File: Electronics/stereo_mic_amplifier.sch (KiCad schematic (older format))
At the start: 26 parts, among them P1 mic_L, P2 mic_R, P3 batt, P4 CONN_01X03, U1 TL072

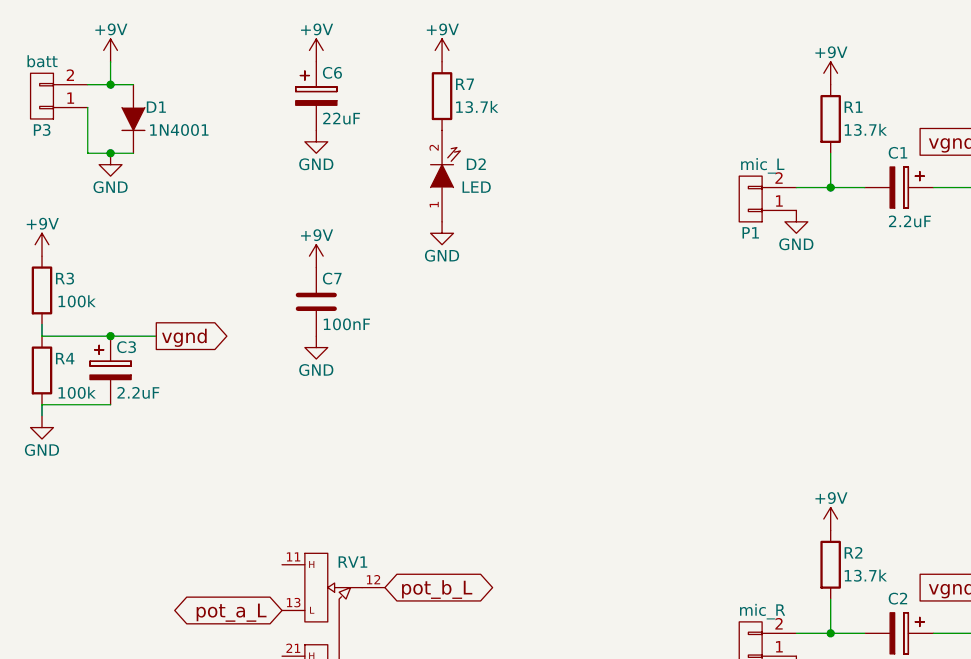
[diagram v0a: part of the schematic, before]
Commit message: Fixed reversed diodes
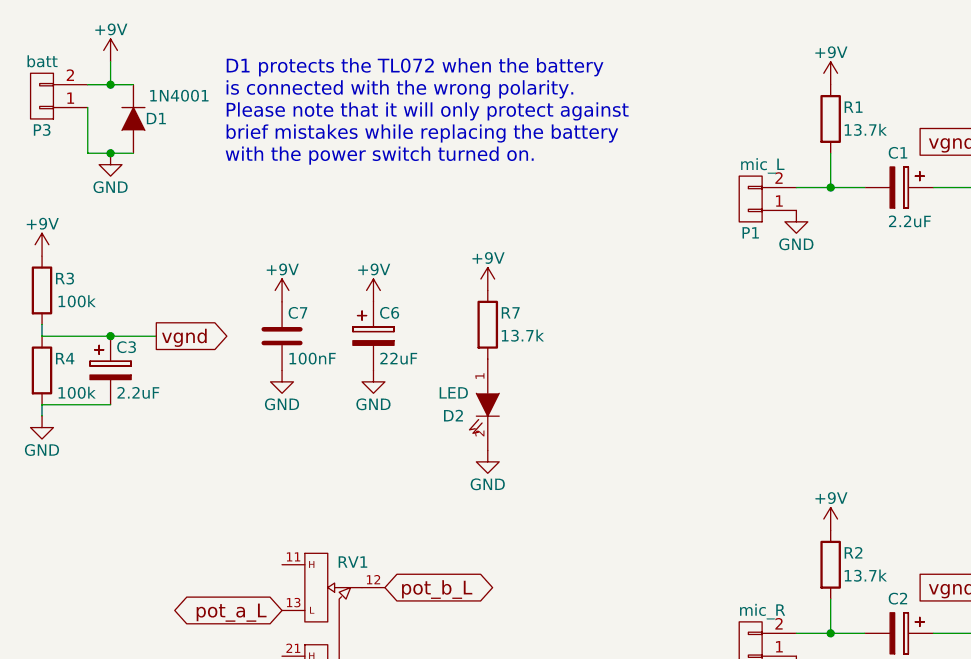
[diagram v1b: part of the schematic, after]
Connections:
- net +9V: now also D1.2 (K); no longer D1.1 (A)
- net GND: now also D1.1 (A), D2.2 (K); no longer D1.2 (K), D2.1 (A)
- net at R7.2: now also D2.1 (A); no longer D2.2 (K)
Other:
- note added: "D1 protects the TL072 when the battery\nis connected with the wrong polarity.\nPlease note that it will only protect against\nbrief mistakes while replacing the battery\nwith the power switch turned on."
- moved on the sheet: C6, C7, D2, R7
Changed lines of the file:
@@
 L LED D2
 U 1 1 5576C5E6
-P 2400 1200
-F 0 "D2" V 2450 1050 50  0000 C CNN
-F 1 "LED" V 2350 1050 50  0000 C CNN
-F 2 "LEDs:LED-5MM" H 2400 1200 60  0001 C CNN
-F 3 "" H 2400 1200 60  0000 C CNN
-	1    2400 1200
-	0    -1   -1   0
+P 2600 2200
+F 0 "D2" V 2650 2050 50  0000 C CNN
+F 1 "LED" V 2550 2050 50  0000 C CNN
+F 2 "LEDs:LED-5MM" H 2600 2200 60  0001 C CNN
+F 3 "" H 2600 2200 60  0000 C CNN
+	1    2600 2200
+	0    1    1    0
 $EndComp
 $Comp
 L +9V #PWR01
 U 1 1 5576C720
-P 1850 1600
-F 0 "#PWR01" H 1850 1450 50  0001 C CNN
-F 1 "+9V" H 1850 1740 50  0000 C CNN
-F 2 "" H 1850 1600 60  0000 C CNN
-F 3 "" H 1850 1600 60  0000 C CNN
-	1    1850 1600
+P 1700 1750
+F 0 "#PWR01" H 1700 1600 50  0001 C CNN
+F 1 "+9V" H 1700 1890 50  0000 C CNN
+F 2 "" H 1700 1750 60  0000 C CNN
+F 3 "" H 1700 1750 60  0000 C CNN
+	1    1700 1750
 	1    0    0    -1
 $EndComp
@@
 L GND #PWR02
 U 1 1 5576C739
-P 1850 1900
-F 0 "#PWR02" H 1850 1650 50  0001 C CNN
-F 1 "GND" H 1850 1750 50  0000 C CNN
-F 2 "" H 1850 1900 60  0000 C CNN
-F 3 "" H 1850 1900 60  0000 C CNN
-	1    1850 1900
+P 1700 2050
+F 0 "#PWR02" H 1700 1800 50  0001 C CNN
+F 1 "GND" H 1700 1900 50  0000 C CNN
+F 2 "" H 1700 2050 60  0000 C CNN
+F 3 "" H 1700 2050 60  0000 C CNN
+	1    1700 2050
 	1    0    0    -1
 $EndComp
@@
 U 1 1 5576C83A
 P 1050 950
-F 0 "D1" V 1000 1050 50  0000 C CNN
-F 1 "1N4001" V 1100 1150 50  0000 C CNN
+F 0 "D1" V 1050 850 50  0000 C CNN
+F 1 "1N4001" V 1150 750 50  0000 C CNN
 F 2 "Discret:D3" H 1050 950 60  0001 C CNN
 F 3 "" H 1050 950 60  0000 C CNN
 	1    1050 950
-	0    1    1    0
+	0    -1   -1   0
 $EndComp
 $Comp
@@
 L CP C6
 U 1 1 5576CEE9
-P 1850 850
-F 0 "C6" H 1875 950 50  0000 L CNN
-F 1 "22uF" H 1875 750 50  0000 L CNN
-F 2 "Discret:C1V8" H 1888 700 30  0001 C CNN
-F 3 "" H 1850 850 60  0000 C CNN
-	1    1850 850
+P 2100 1900
+F 0 "C6" H 2125 2000 50  0000 L CNN
+F 1 "22uF" H 2125 1800 50  0000 L CNN
+F 2 "Discret:C1V8" H 2138 1750 30  0001 C CNN
+F 3 "" H 2100 1900 60  0000 C CNN
+	1    2100 1900
 	1    0    0    -1
 $EndComp
@@
 L C C7
 U 1 1 55798F95
-P 1850 1750
-F 0 "C7" H 1875 1850 50  0000 L CNN
-F 1 "100nF" H 1875 1650 50  0000 L CNN
-F 2 "Capacitors_ThroughHole:C_Disc_D7.5_P5" H 1888 1600 30  0001 C CNN
-F 3 "" H 1850 1750 60  0000 C CNN
-	1    1850 1750
+P 1700 1900
+F 0 "C7" H 1725 2000 50  0000 L CNN
+F 1 "100nF" H 1725 1800 50  0000 L CNN
+F 2 "Capacitors_ThroughHole:C_Disc_D7.5_P5" H 1738 1750 30  0001 C CNN
+F 3 "" H 1700 1900 60  0000 C CNN
+	1    1700 1900
 	1    0    0    -1
 $EndComp
@@
 L GND #PWR012
 U 1 1 557A04B1
-P 1850 1000
-F 0 "#PWR012" H 1850 750 50  0001 C CNN
-F 1 "GND" H 1850 850 50  0000 C CNN
-F 2 "" H 1850 1000 60  0000 C CNN
-F 3 "" H 1850 1000 60  0000 C CNN
-	1    1850 1000
+P 2100 2050
+F 0 "#PWR012" H 2100 1800 50  0001 C CNN
+F 1 "GND" H 2100 1900 50  0000 C CNN
+F 2 "" H 2100 2050 60  0000 C CNN
+F 3 "" H 2100 2050 60  0000 C CNN
+	1    2100 2050
 	1    0    0    -1
 $EndComp
@@
 L +9V #PWR013
 U 1 1 557A04EE
-P 1850 700
-F 0 "#PWR013" H 1850 550 50  0001 C CNN
-F 1 "+9V" H 1850 840 50  0000 C CNN
-F 2 "" H 1850 700 60  0000 C CNN
-F 3 "" H 1850 700 60  0000 C CNN
-	1    1850 700
+P 2100 1750
+F 0 "#PWR013" H 2100 1600 50  0001 C CNN
+F 1 "+9V" H 2100 1890 50  0000 C CNN
+F 2 "" H 2100 1750 60  0000 C CNN
+F 3 "" H 2100 1750 60  0000 C CNN
+	1    2100 1750
 	1    0    0    -1
 $EndComp
@@
 L R R7
 U 1 1 557A0E47
-P 2400 850
-F 0 "R7" H 2500 900 50  0000 C CNN
-F 1 "13.7k" H 2550 800 50  0000 C CNN
-F 2 "Resistors_ThroughHole:Resistor_Horizontal_RM10mm" V 2330 850 30  0001 C CNN
-F 3 "" H 2400 850 30  0000 C CNN
-	1    2400 850
+P 2600 1850
+F 0 "R7" H 2700 1900 50  0000 C CNN
+F 1 "13.7k" H 2750 1800 50  0000 C CNN
+F 2 "Resistors_ThroughHole:Resistor_Horizontal_RM10mm" V 2530 1850 30  0001 C CNN
+F 3 "" H 2600 1850 30  0000 C CNN
+	1    2600 1850
 	1    0    0    -1
 $EndComp
@@
 L +9V #PWR014
 U 1 1 557A119D
-P 2400 700
-F 0 "#PWR014" H 2400 550 50  0001 C CNN
-F 1 "+9V" H 2400 840 50  0000 C CNN
-F 2 "" H 2400 700 60  0000 C CNN
-F 3 "" H 2400 700 60  0000 C CNN
-	1    2400 700
+P 2600 1700
+F 0 "#PWR014" H 2600 1550 50  0001 C CNN
+F 1 "+9V" H 2600 1840 50  0000 C CNN
+F 2 "" H 2600 1700 60  0000 C CNN
+F 3 "" H 2600 1700 60  0000 C CNN
+	1    2600 1700
 	1    0    0    -1
 $EndComp
@@
 L GND #PWR015
 U 1 1 557A1314
-P 2400 1400
-F 0 "#PWR015" H 2400 1150 50  0001 C CNN
-F 1 "GND" H 2400 1250 50  0000 C CNN
-F 2 "" H 2400 1400 60  0000 C CNN
-F 3 "" H 2400 1400 60  0000 C CNN
-	1    2400 1400
+P 2600 2400
+F 0 "#PWR015" H 2600 2150 50  0001 C CNN
+F 1 "GND" H 2600 2250 50  0000 C CNN
+F 2 "" H 2600 2400 60  0000 C CNN
+F 3 "" H 2600 2400 60  0000 C CNN
+	1    2600 2400
 	1    0    0    -1
 $EndComp
@@
 	1    0    0    -1
 $EndComp
+Text Notes 1450 1150 0    60   ~ 0
+D1 protects the TL072 when the battery\nis connected with the wrong polarity.\nPlease note that it will only protect against\nbrief mistakes while replacing the battery\nwith the power switch turned on.
 $EndSCHEMATC
